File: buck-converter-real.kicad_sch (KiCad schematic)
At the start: 80 parts, among them J1 USB_C_Receptacle_USB2.0_16P, J10 I2C1, J11 SWD, J12 Conn_01x04, J13 Conn_01x15, J14 Boot, J2 SOL 24V, J3 Battery out (3V6-4V2) NiMH 3S, J4 POWER, J5 Barrel_Jack_MountingPin, J6 DM3CS-SF, J7 UART 1, J8 I2C1, J9 SWD, Q1 CSD18540Q5B - 60-V, SW2 SW_Omron_B3FS, U1 AP2112K-3.3 (3V3 LDO), U2 CH32V203K8T6, U5 LM5109BMA (Mosfet Driver), U6 78L12L (12V LDO) (35V max), Y1 8MHz 20pF

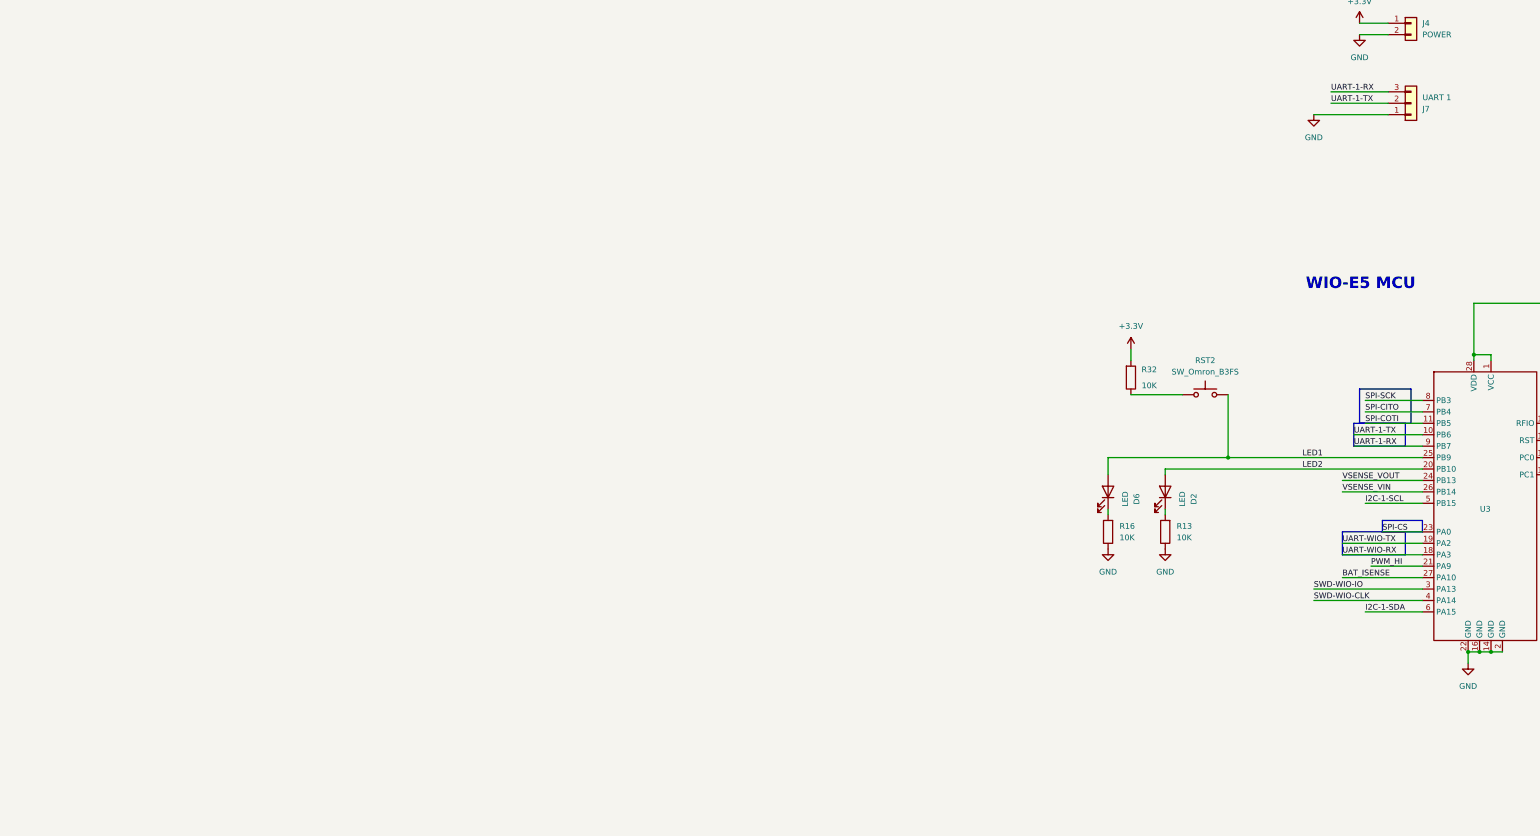
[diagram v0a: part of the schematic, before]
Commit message: Fix 3V3 to radio
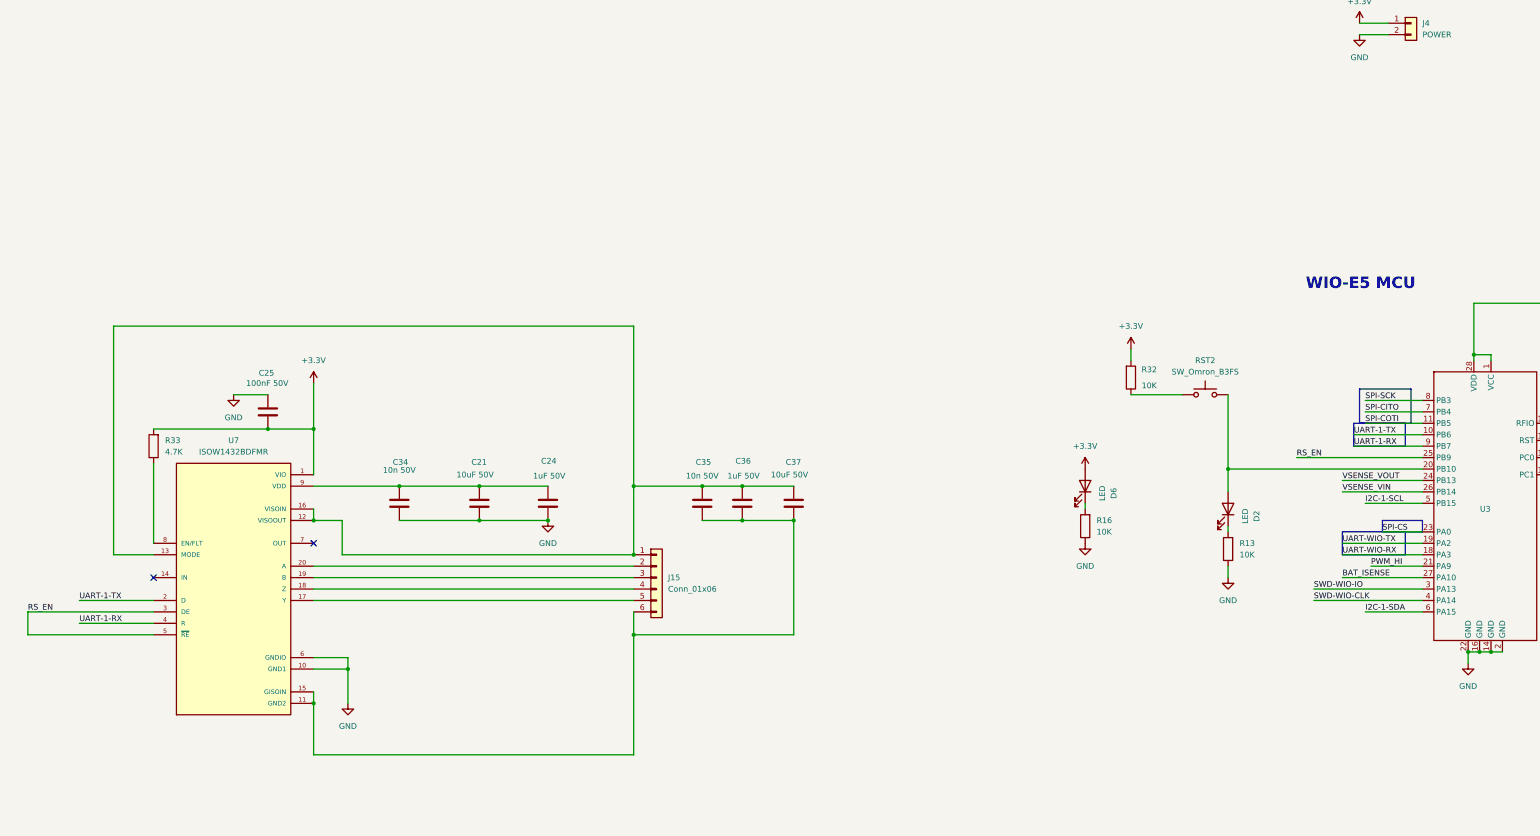
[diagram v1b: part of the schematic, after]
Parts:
- removed J7: UART 1, Connector_PinHeader_2.54mm:PinHeader_1x03_P2.54mm_Vertical, symbol Connector_Generic:Conn_01x03
- added C21, C37: 10uF 50V, Capacitor_SMD:C_0603_1608Metric, symbol Device:C
- added C24, C36: 1uF 50V, Capacitor_SMD:C_0603_1608Metric, symbol Device:C
- added C25: 100nF 50V, Capacitor_SMD:C_0603_1608Metric, symbol Device:C
- added C34, C35: 10n 50V, Capacitor_SMD:C_0805_2012Metric_Pad1.18x1.45mm_HandSolder, symbol PCM_Capacitor_AKL:C_0805
- added J15: Conn_01x06, Connector_JST:JST_PH_B6B-PH-SM4-TB_1x06-1MP_P2.00mm_Vertical, symbol Connector_Generic:Conn_01x06
- added R33: 4.7K, Resistor_SMD:R_0805_2012Metric_Pad1.20x1.40mm_HandSolder, symbol PCM_Resistor_AKL:R_0805
- added U7: ISOW1432BDFMR, buck-forest:SOIC127P1030X355-20N, symbol ISOW1432BDFMR:ISOW1432BDFMR
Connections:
- net +3.3V: now also D6.2 (A), C25.2, R33.1, U7.1 (VIO)
- net GND: now also C21.2, C24.2, C25.1, C34.2, U7.10 (GND1), U7.6 (GNDIO)
- net UART-1-RX: now also U7.4 (R)
- net UART-1-TX: now also U7.2 (D)
- removed net LED1: D6.2 (A), RST2.2, U3.25 (PB9)
- net LED2: no longer names the net of D2.2 (A), U3.20 (PB10)
- net LED2: now also RST2.2
- new net: C21.1, C24.1, C34.1, U7.9 (VDD)
- new net: C35.2, C36.2, C37.2, J15.6 (Pin_6), U7.11 (GND2), U7.15 (GISOIN)
- new net: C35.1, C36.1, C37.1, J15.1 (Pin_1), U7.12 (VISOOUT), U7.13 (MODE), U7.16 (VISOIN)
- new net: J15.5 (Pin_5), U7.17 (Y)
- new net: J15.4 (Pin_4), U7.18 (Z)
- new net: J15.3 (Pin_3), U7.19 (B)
- new net: J15.2 (Pin_2), U7.20 (A)
- new net: R33.2, U7.8 (EN/FLT)
- new net RS_EN: U3.25 (PB9), U7.3 (DE), U7.5 (~{RE})
- no-connect marks 5 -> 7
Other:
- moved on the sheet: D2, D6, R13, R16

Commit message: Rearange, replace 12v ldo with buck
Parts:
- removed C19: 100nF 50V, Capacitor_SMD:C_0805_2012Metric_Pad1.18x1.45mm_HandSolder, symbol PCM_Capacitor_AKL:C_0805
- removed C21, C37: 10uF 50V, Capacitor_SMD:C_0603_1608Metric, symbol Device:C
- removed C24, C36: 1uF 50V, Capacitor_SMD:C_0603_1608Metric, symbol Device:C
- removed C25: 100nF 50V, Capacitor_SMD:C_0603_1608Metric, symbol Device:C
- removed C34, C35: 10n 50V, Capacitor_SMD:C_0805_2012Metric_Pad1.18x1.45mm_HandSolder, symbol PCM_Capacitor_AKL:C_0805
- removed J14: Boot, Connector_PinHeader_2.54mm:PinHeader_1x02_P2.54mm_Vertical, symbol Connector_Generic:Conn_01x02
- removed J15: Conn_01x06, Connector_JST:JST_PH_B6B-PH-SM4-TB_1x06-1MP_P2.00mm_Vertical, symbol Connector_Generic:Conn_01x06
- removed R33: 4.7K, Resistor_SMD:R_0805_2012Metric_Pad1.20x1.40mm_HandSolder, symbol PCM_Resistor_AKL:R_0805
- removed U6: 78L12L (12V LDO) (35V max), Package_TO_SOT_SMD:SOT-89-3, symbol PCM_Voltage_Regulator_AKL:AS78L12RTR-G1
- removed U7: ISOW1432BDFMR, buck-forest:SOIC127P1030X355-20N, symbol ISOW1432BDFMR:ISOW1432BDFMR
- added C39: 2.2uF, Capacitor_SMD:C_0603_1608Metric, symbol Device:C
- added C40: 15uF, Capacitor_SMD:C_0805_2012Metric, symbol Device:C
- added C41: 100nF, Capacitor_SMD:C_0603_1608Metric, symbol Device:C
- added L3: 56 uH, Inductor_SMD:L_TDK_VLS6045EX_VLS6045AF, symbol Device:L
- added R35: 309, Capacitor_SMD:C_0603_1608Metric, symbol Device:R_US
- added R36: 22.1, Capacitor_SMD:C_0603_1608Metric, symbol Device:R_US
- added TP1: BOOT, TestPoint:TestPoint_Pad_D1.0mm, symbol Connector:TestPoint
- added TP2: 3V3, TestPoint:TestPoint_Pad_D1.0mm, symbol Connector:TestPoint
- added U4: LMR51603XDBVR, Package_TO_SOT_SMD:SOT-23-6, symbol Regulator_Switching:LMR51430
- J11: footprint Connector_PinHeader_2.54mm:PinHeader_1x04_P2.54mm_Vertical -> Connector_JST:JST_SH_BM04B-SRSS-TB_1x04-1MP_P1.00mm_Vertical
- J9: footprint Connector_JST:JST_PH_B4B-PH-K_1x04_P2.00mm_Vertical -> Connector_JST:JST_SH_BM04B-SRSS-TB_1x04-1MP_P1.00mm_Vertical
- L2: footprint buck-forest:L_10.4x10.4_H4.8 -> Inductor_SMD:L_Sunlord_SWPA8040S
- R11, R12, R13, R14, R15, R16, R17, R18, R19, R20, R21, R22, R23, R24, R25, R26, R27, R28, R29, R30, R31, R32: symbol PCM_Resistor_AKL:R_0805 -> Device:R_US
- U1: footprint PCM_SparkFun-Semiconductor-Standard:SOT23-5 -> Package_TO_SOT_SMD:SOT-23-5
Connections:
- net +3.3V: now also J11.2 (Pin_2), J9.2 (Pin_2), TP2.1; no longer J11.1 (Pin_1), J9.1 (Pin_1), U3.28 (VDD)
- net CH-SWD-CLK: now also J11.4 (Pin_4); no longer J11.2 (Pin_2)
- net GND: now also J11.1 (Pin_1), J9.1 (Pin_1), C39.2, C40.2, R36.2, U4.2 (GND); no longer J10.MP (Shield), J11.4 (Pin_4), J8.MP (Shield), J9.4 (Pin_4)
- net SWD-WIO-CLK: now also J9.4 (Pin_4); no longer J9.3 (Pin_3)
- net SWD-WIO-IO: now also J9.3 (Pin_3); no longer J9.2 (Pin_2)
- net Solar In: now also C39.1, U4.4 (EN), U4.5 (VIN)
- net at R21.1, U2.31 (PB8/BOOT0): now also TP1.1
- net at U2.14 (PB0/ADC8): now also J13.12 (Pin_12); no longer J13.14 (Pin_14)
- net at U2.15 (PB1/ADC9): now also J13.14 (Pin_14); no longer J13.15 (Pin_15)
- net at U2.18 (PA8): now also J13.15 (Pin_15); no longer J13.12 (Pin_12)
- net 12V-OUT-LDO renamed 12V-buck
- net 12V-buck: now also C40.1, L3.1, R35.1
- new net: C41.1, U4.1 (CB)
- new net: R35.2, R36.1, U4.3 (FB)
- new net: C41.2, L3.2, U4.6 (SW)
- no-connect marks 7 -> 8
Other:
- note added: "CH32 Power - Make optional both? pull down EN from WIO?"
- note added: "Isolated RS422/482"
- moved on the sheet: D13, J11

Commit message: Add bucks/rs485/422
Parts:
- added C16, C19, C21: 1n, Capacitor_SMD:C_0603_1608Metric, symbol Device:C
- added C34: 100nF, Capacitor_SMD:C_0805_2012Metric_Pad1.18x1.45mm_HandSolder, symbol PCM_Capacitor_AKL:C_0805
- added C38, C42, C43: 22uF 10V X7R/X5R 0805, Capacitor_SMD:C_0805_2012Metric_Pad1.18x1.45mm_HandSolder, symbol PCM_Capacitor_AKL:C_0805
- added C44: 100nF 50V, Capacitor_SMD:C_0805_2012Metric_Pad1.18x1.45mm_HandSolder, symbol PCM_Capacitor_AKL:C_0805
- added J7: Conn_01x06, symbol Connector_Generic:Conn_01x06
- added L4: 1uH lsat@5A 30mOhm AOTA-N252010S-1R0MT, Inductor_SMD:L_1008_2520Metric, symbol Device:L
- added R33, R34, R38, R39, R40: 0, Resistor_SMD:R_0805_2012Metric_Pad1.20x1.40mm_HandSolder, symbol Device:R_US
- added R41: 732k, Resistor_SMD:R_0603_1608Metric, symbol Device:R_US
- added R42: 100k, Resistor_SMD:R_0603_1608Metric, symbol Device:R_US
- added R43: 0, Resistor_SMD:R_0603_1608Metric, symbol Device:R_US
- added U6: TPT482-VS2R, Package_SO:MSOP-10_3x3mm_P0.5mm, symbol forest-ch:TPT482-VS2R
- added U8: TPS61022, Package_DFN_QFN:Texas_RWU0007A_VQFN-7_2x2mm_P0.5mm, symbol Converter_DCDC:TPS61022
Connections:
- net +3.3V: now also R33.1, U6.10 (VCC); no longer D6.2 (A)
- net BAT_ISENSE: now also R39.2; no longer U3.27 (PA10)
- net GND: now also C16.2, C19.2, C21.2, C34.2, C38.2, C42.2, C43.2, C44.2, J7.6 (Pin_6), R42.2, U6.5 (GND), U8.1 (GND)
- net UART-1-RX: now also U6.1 (R)
- net UART-1-TX: now also U6.4 (D)
- net VSENSE_VIN: now also R38.2; no longer U3.26 (PB14)
- net VSENSE_VOUT: now also R40.2; no longer U3.24 (PB13)
- net at C14.1, D12.1 (K), D13.1 (K)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: now also L4.1, R43.1, U8.7 (VIN)
- net RS_EN renamed Receiver Output Enable
- net Receiver Output Enable: now also U6.2 (RE)
- new net: C44.1, J7.1 (Pin_1), R33.2, R34.2
- new net: L4.2, U8.2 (SW)
- new net: C16.1, R38.1, U3.26 (PB14)
- new net: C19.1, R39.1, U3.27 (PA10)
- new net: R43.2, U8.6 (MODE)
- new net: C21.1, R40.1, U3.24 (PB13)
- new net: R41.2, R42.1, U8.4 (FB)
- new net: J7.5 (Pin_5), U6.6 (Y)
- new net: J7.4 (Pin_4), U6.7 (Z)
- new net: J7.3 (Pin_3), U6.8 (B)
- new net: J7.2 (Pin_2), U6.9 (A)
- new net +5V: C34.1, C38.1, C42.1, C43.1, R34.1, R41.1, U8.3 (VOUT)
- new net 5V EN: U8.5 (EN)
- new net Receiver Input Enable: U3.20 (PB10), U6.3 (DE)
- now unconnected: D2.2 (A), RST2.2
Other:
- note added: "10-16V X5R or X7R input/output caps"
- note added: "5V Boost"
- note added: "@ 400 mAnom"
- note added: "Check if need to remove GND for RS485/422"
- note added: "Default SMD size: 0603 unless otherwise marked"
- note added: "I2C GPIO for EN?"
- note added: "RS422/482"
- note removed: "@ ??? mAnom"
- note removed: "Default SMD size: 0806 unless otherwise marked"
- note removed: "Isolated RS422/482"
- moved on the sheet: D2, D6, J10, J12, J4, J8, J9, R13, R16, R27, R28, R30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

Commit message: Buck layout, add headers.
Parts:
- removed SW2: SW_Omron_B3FS, Button_Switch_SMD:SW_SPST_Omron_B3FS-100xP, symbol Switch:SW_Omron_B3FS
- added C45: 10uF 10V X7R/X5R 0805, Capacitor_SMD:C_0805_2012Metric_Pad1.18x1.45mm_HandSolder, symbol PCM_Capacitor_AKL:C_0805
- added J14: Conn_01x04, Connector_JST:JST_XH_S4B-XH-A-1_1x04_P2.50mm_Horizontal, symbol Connector_Generic:Conn_01x04
- added J15: Conn_01x06, Connector_JST:JST_XH_S6B-XH-A_1x06_P2.50mm_Horizontal, symbol Connector_Generic:Conn_01x06
- added R37, R44: 120, Capacitor_SMD:C_0603_1608Metric, symbol Device:R_US
- added R45, R46: 0, Resistor_SMD:R_0603_1608Metric, symbol Device:R_US
- added RST3: SW_Omron_B3FS, Button_Switch_SMD:SW_SPST_PTS647_Sx38, symbol Switch:SW_Omron_B3FS
- added U10: TLV75733PDRV, Package_SON:WSON-6-1EP_2x2mm_P0.65mm_EP1x1.6mm, symbol Regulator_Linear:TLV75733PDRV
- added U7: TCAN3414DDFR, Package_TO_SOT_SMD:TSOT-23-8, symbol Interface_CAN_LIN:TCAN337G
- RST2: footprint Button_Switch_SMD:SW_SPST_Omron_B3FS-100xP -> Button_Switch_SMD:SW_SPST_PTS647_Sx38
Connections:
- net +3.3V: now also U10.1 (OUT), U7.3 (VCC); no longer U1.5 (VOUT)
- net GND: now also C45.2, R37.2, R44.1, RST3.2, U10.3 (GND), U10.7 (GND), U7.2 (GND); no longer U1.2 (GND)
- net at C14.1, D12.1 (K), D13.1 (K)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: now also C45.1, U10.4 (EN), U10.6 (IN); no longer U1.1 (VIN), U1.3 (EN)
- net at J1.A6 (D+), J1.B6 (D+), U2.22 (PA12/USB1DP): now also R45.1
- net at J1.A7 (D-), J1.B7 (D-), U2.21 (PA11/USB1DM): now also R46.1
- net at C32.2, R22.2, U2.4 (NRST): now also RST3.1
- new net: R37.1, U7.7 (CANH)
- new net: R45.2, U7.1 (TXD)
- new net: R46.2, U7.4 (RXD)
- new net: R44.2, U7.6 (CANL)
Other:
- note removed: "Check if need to remove GND for RS485/422"

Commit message: Change buck IC
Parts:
- removed C40: 15uF, Capacitor_SMD:C_0805_2012Metric, symbol Device:C
- added C46, C47: 22uF 10V X7R/X5R 0805, Capacitor_SMD:C_0805_2012Metric_Pad1.18x1.45mm_HandSolder, symbol PCM_Capacitor_AKL:C_0805
- added C48: 100nF, Capacitor_SMD:C_0603_1608Metric, symbol Device:C
- added R47: 1.5m, Capacitor_SMD:C_0603_1608Metric, symbol Device:R_US
- added R48: 100k, Capacitor_SMD:C_0603_1608Metric, symbol Device:R_US
- L3: value 56 uH -> 68u; footprint Inductor_SMD:L_TDK_VLS6045EX_VLS6045AF -> Inductor_SMD:L_Chilisin_BWVS00606020
- R35: value 309 -> 309k
- R36: value 22.1 -> 22.1k
- U4: value LMR51603XDBVR -> LMR51610YDBVR
- U5: value LM5109BMA (Mosfet Driver) -> LM5109BMA/NOPB
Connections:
- net 12V-buck: now also C46.1, C47.1, C48.2
- net GND: now also C46.2, C47.2, C48.1, R48.2
- net Solar In: now also R47.1; no longer U4.4 (EN)
- new net: R47.2, R48.1, U4.4 (EN)
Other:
- moved on the sheet: C10, C11, C12, C13, C14, C15, C16, C17, C18, C19, C20, C21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

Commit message: Remapping board
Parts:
- removed J2: SOL 24V, Connector_AMASS:AMASS_XT30UPB-F_1x02_P5.0mm_Vertical, symbol Connector:Conn_01x02_Socket
- removed J3: Battery out (3V6-4V2) NiMH 3S, Connector_AMASS:AMASS_XT30UPB-F_1x02_P5.0mm_Vertical, symbol Connector:Conn_01x02_Socket
- removed J5: Barrel_Jack_MountingPin, Connector_BarrelJack:BarrelJack_CUI_PJ-063AH_Horizontal, symbol Connector:Barrel_Jack_MountingPin
- L2: value 10uH ±20% 18mΩ Molded -> 10uH 18mOhm
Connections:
- net +BATT: now also J15.1 (Pin_1), J15.2 (Pin_2), J15.3 (Pin_3); no longer C22.1, C23.1, L2.1, R12.1
- net BAT_ISENSE: now also J15.4 (Pin_4), J15.5 (Pin_5), J15.6 (Pin_6)
- net GND: now also C22.1, C23.1, J14.1 (Pin_1), J14.2 (Pin_2), L2.2, R12.1, U10.2 (NC), U10.5 (NC)
- net Solar +: now also J14.3 (Pin_3), J14.4 (Pin_4)
- net at C17.1, D3.1 (K), Q1.1 (S)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: now also L2.1; no longer L2.2
- net BATT-IN: now reaches C14.1, C45.1, D12.1 (K), D13.1 (K), L4.1, R43.1, U10.4 (EN), U10.6 (IN), U8.7 (VIN)
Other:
- moved on the sheet: C12, C22, C23, C44, J14, J15, J7, L2, Q1, R1, R33, R34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
